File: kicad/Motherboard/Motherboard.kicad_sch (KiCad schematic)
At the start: 72 parts, among them J1 USB_C_Receptacle_USB2.0, J10 Conn_01x08_Pin, J11 Conn_01x08_Pin, J12 Conn_01x08_Pin, J13 Conn_01x08_Pin, J2 Conn_01x02_Pin, J3 Conn_01x04_Pin, J4 Conn_01x04_Pin, J5 Conn_01x02_Pin, J6 Conn_01x08_Pin, J7 Conn_01x08_Pin, J8 Conn_01x08_Pin, J9 Conn_01x08_Pin, Q1 DMN3404L, SW1 Reset, SW2 Boot, U1 ESP32-S2-SOLO, U2 LD1117S33TR_SOT223, U3 TCA9535RTWR, U4 TCA9535RTWR, U5 TCA9535RTWR, U6 TCA9535RTWR, U7 TMC2209-LA, U8 TMC2209-LA, U9 LM2575-5.0BT

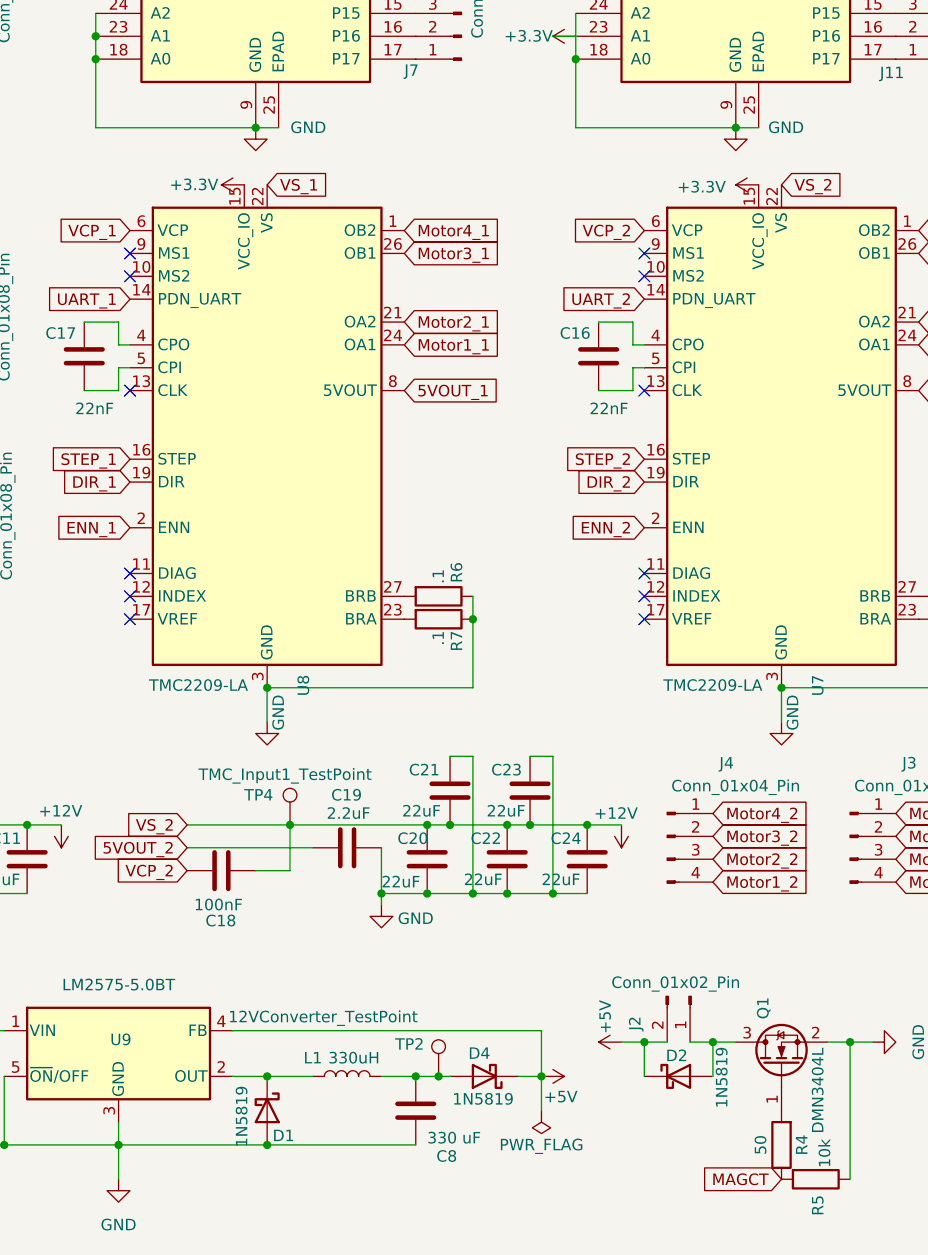
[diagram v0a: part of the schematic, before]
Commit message: finalized schematic
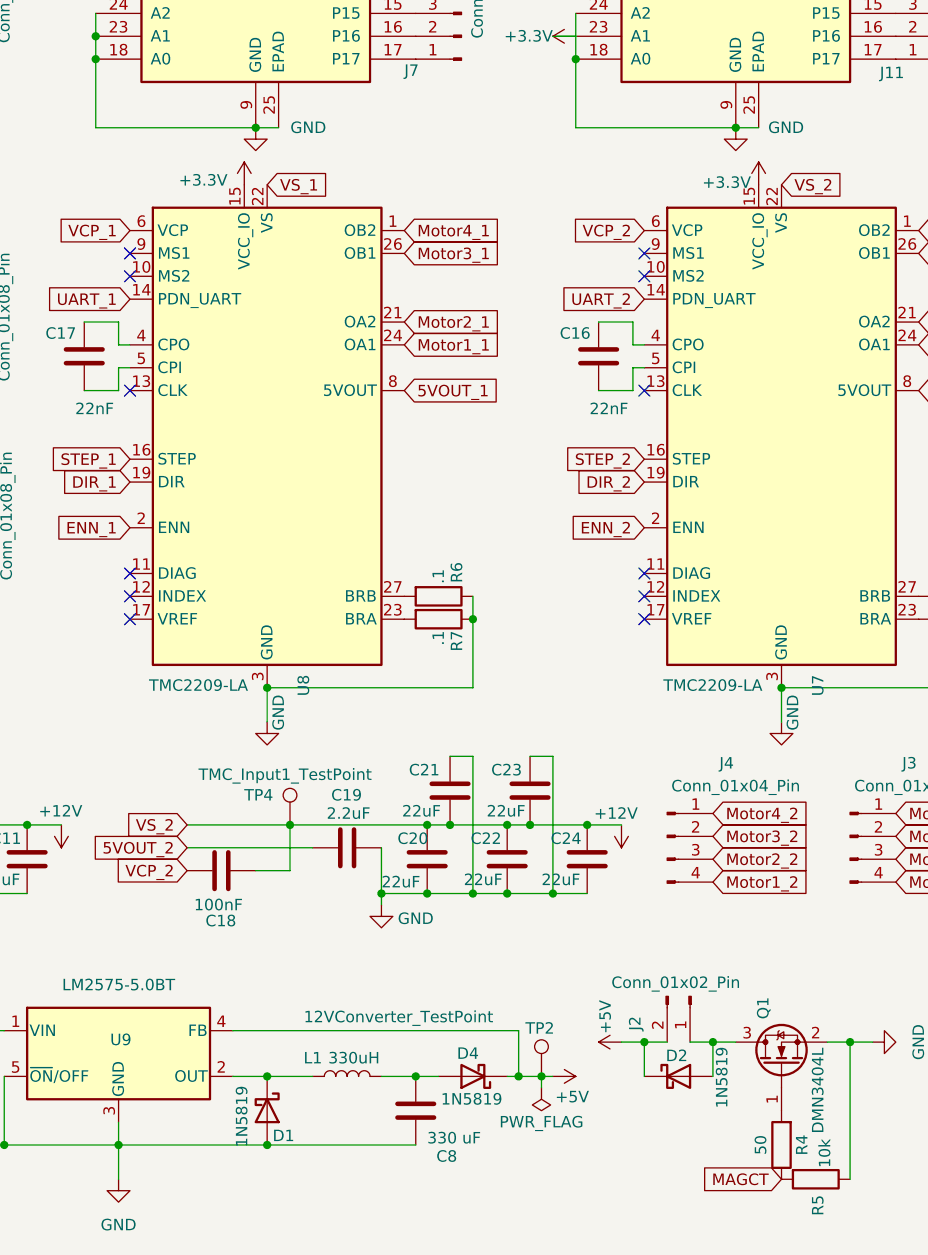
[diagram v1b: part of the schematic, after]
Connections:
- net +5V: now also TP2.1
- net at C8.1, D4.2 (A), L1.2: no longer TP2.1
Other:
- moved on the sheet: D4

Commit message: best layout
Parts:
- removed TP5: TMC_Input2_TestPoint, TestPoint:TestPoint_Pad_1.5x1.5mm, symbol Connector:TestPoint
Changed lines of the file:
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@@
-	)
-	(symbol
-		(lib_id "Connector:TestPoint")
-		(at 36.83 149.86 0)
-		(unit 1)
-		(exclude_from_sim no)
-		(in_bom yes)
-		(on_board yes)
-		(dnp no)
-		(property "Reference" "TP5"
-			(at 31.75 146.812 0)
-			(effects
-				(font
-					(size 1.27 1.27)
-				)
-				(justify left)
-			)
-		)
-		(property "Value" "TMC_Input2_TestPoint"
-			(at 26.416 144.272 0)
-			(effects
-				(font
-					(size 1.27 1.27)
-				)
-				(justify left)
-			)
-		)
-		(property "Footprint" "TestPoint:TestPoint_Pad_1.5x1.5mm"
-			(at 41.91 149.86 0)
-			(effects
-				(font
-					(size 1.27 1.27)
-				)
-				(hide yes)
-			)
-		)
-		(property "Datasheet" "~"
-			(at 41.91 149.86 0)
-			(effects
-				(font
-					(size 1.27 1.27)
-				)
-				(hide yes)
-			)
-		)
-		(property "Description" "test point"
-			(at 36.83 149.86 0)
-			(effects
-				(font
-					(size 1.27 1.27)
-				)
-				(hide yes)
-			)
-		)
-		(pin "1"
-		)
-		(instances
-			(project "Motherboard"
-				(path "/6e7606c8-26d5-4d26-b509-210c4758a44d"
-					(reference "TP5")
-					(unit 1)
-				)
-			)
-		)
 	)
 	(symbol

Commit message: done agian
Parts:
- added H1, H2, H3, H4: MountingHole, symbol Mechanical:MountingHole

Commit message: Done and broke my computer
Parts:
- C7: footprint Capacitor_SMD:C_0805_2012Metric_Pad1.18x1.45mm_HandSolder -> Capacitor_SMD:C_1210_3225Metric_Pad1.33x2.70mm_HandSolder
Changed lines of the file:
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@@
 			)
 		)
-		(property "Footprint" "Capacitor_SMD:C_0805_2012Metric_Pad1.18x1.45mm_HandSolder"
+		(property "Footprint" "Capacitor_SMD:C_1210_3225Metric_Pad1.33x2.70mm_HandSolder"
 			(at 56.8452 182.88 0)
 			(effects

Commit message: FML
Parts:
- U7, U8: footprint Package_DFN_QFN:TQFN-32-1EP_5x5mm_P0.5mm_EP3.4x3.4mm_ThermalVias -> Package_DFN_QFN:TQFN-28-1EP_5x5mm_P0.5mm_EP3.25x3.25mm_ThermalVias
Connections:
- net GND: now also U7.29 (EPAD), U8.29 (EPAD)
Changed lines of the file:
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@@
 	)
 	(junction
+		(at 151.13 134.62)
+		(diameter 0)
+		(color 0 0 0 0)
+	)
+	(junction
 		(at 26.67 179.07)
 		(diameter 0)
@@
 	)
 	(junction
+		(at 96.52 134.62)
+		(diameter 0)
+		(color 0 0 0 0)
+	)
+	(junction
+		(at 154.94 134.62)
+		(diameter 0)
+		(color 0 0 0 0)
+	)
+	(junction
 		(at 77.47 64.77)
 		(diameter 0)
@@
 	)
 	(junction
+		(at 97.79 134.62)
+		(diameter 0)
+		(color 0 0 0 0)
+	)
+	(junction
 		(at 96.52 185.42)
 		(diameter 0)
@@
 	)
 	(junction
+		(at 93.98 134.62)
+		(diameter 0)
+		(color 0 0 0 0)
+	)
+	(junction
 		(at 240.03 24.13)
 		(diameter 0)
@@
 	)
 	(junction
-		(at 153.67 134.62)
-		(diameter 0)
-		(color 0 0 0 0)
-	)
-	(junction
 		(at 124.46 177.8)
 		(diameter 0)
@@
 	)
 	(junction
-		(at 119.38 157.48)
+		(at 153.67 134.62)
 		(diameter 0)
 		(color 0 0 0 0)
 	)
 	(junction
-		(at 96.52 134.62)
+		(at 119.38 157.48)
 		(diameter 0)
 		(color 0 0 0 0)
@@
 	(wire
 		(pts
+			(xy 147.32 134.62) (xy 151.13 134.62)
+		)
+		(stroke
+			(width 0)
+			(type default)
+		)
+	)
+	(wire
+		(pts
+			(xy 97.79 134.62) (xy 119.38 134.62)
+		)
+		(stroke
+			(width 0)
+			(type default)
+		)
+	)
+	(wire
+		(pts
 			(xy 227.33 31.75) (xy 227.33 36.83)
 		)
@@
 	(wire
 		(pts
+			(xy 154.94 134.62) (xy 176.53 134.62)
+		)
+		(stroke
+			(width 0)
+			(type default)
+		)
+	)
+	(wire
+		(pts
 			(xy 124.46 172.72) (xy 124.46 177.8)
 		)
@@
 	(wire
 		(pts
-			(xy 132.08 149.86) (xy 135.89 149.86)
+			(xy 90.17 134.62) (xy 93.98 134.62)
 		)
 		(stroke
@@
 	(wire
 		(pts
-			(xy 201.93 33.02) (xy 199.39 33.02)
+			(xy 132.08 149.86) (xy 135.89 149.86)
 		)
 		(stroke
@@
 	(wire
 		(pts
-			(xy 119.38 134.62) (xy 96.52 134.62)
+			(xy 201.93 33.02) (xy 199.39 33.02)
 		)
 		(stroke
@@
 	(wire
 		(pts
+			(xy 93.98 134.62) (xy 96.52 134.62)
+		)
+		(stroke
+			(width 0)
+			(type default)
+		)
+	)
+	(wire
+		(pts
 			(xy 182.88 138.43) (xy 191.77 138.43)
 		)
@@
 	(wire
 		(pts
-			(xy 176.53 134.62) (xy 153.67 134.62)
+			(xy 259.08 152.4) (xy 259.08 154.94)
 		)
 		(stroke
@@
 	(wire
 		(pts
-			(xy 259.08 152.4) (xy 259.08 154.94)
+			(xy 151.13 134.62) (xy 153.67 134.62)
 		)
 		(stroke
@@
 	(wire
 		(pts
+			(xy 96.52 134.62) (xy 97.79 134.62)
+		)
+		(stroke
+			(width 0)
+			(type default)
+		)
+	)
+	(wire
+		(pts
 			(xy 55.88 182.88) (xy 55.88 185.42)
 		)
@@
 	(wire
 		(pts
+			(xy 153.67 134.62) (xy 154.94 134.62)
+		)
+		(stroke
+			(width 0)
+			(type default)
+		)
+	)
+	(wire
+		(pts
 			(xy 109.22 158.75) (xy 109.22 157.48)
 		)
@@
 			)
 		)
-		(property "Footprint" "Package_DFN_QFN:TQFN-32-1EP_5x5mm_P0.5mm_EP3.4x3.4mm_ThermalVias"
+		(property "Footprint" "Package_DFN_QFN:TQFN-28-1EP_5x5mm_P0.5mm_EP3.25x3.25mm_ThermalVias"
 			(at 153.67 147.32 0)
 			(effects
@@
 		(pin "7"
 		)
+		(pin "29"
+		)
 		(instances
 			(project "Motherboard"
@@
 			)
 		)
-		(property "Footprint" "Package_DFN_QFN:TQFN-32-1EP_5x5mm_P0.5mm_EP3.4x3.4mm_ThermalVias"
+		(property "Footprint" "Package_DFN_QFN:TQFN-28-1EP_5x5mm_P0.5mm_EP3.25x3.25mm_ThermalVias"
 			(at 96.52 147.32 0)
 			(effects
@@
 		(pin "7"
 		)
+		(pin "29"
+		)
 		(instances

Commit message: added new parts
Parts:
- removed H1, H2, H3, H4: MountingHole, symbol Mechanical:MountingHole
- added U10, U11: TMC2209-LA, Package_DFN_QFN:VQFN-28-1EP_5x5mm_P0.5mm_EP3.7x3.7mm_ThermalVias, symbol Driver_Motor:TMC2209-LA
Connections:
- net GND: no longer U3.18 (A0), U3.23 (A1), U3.24 (A2), U3.25 (EPAD), U4.18 (A0), U4.23 (A1), U4.25 (EPAD), U5.18 (A0), U5.24 (A2), U5.25 (EPAD), U6.23 (A1), U6.24 (A2), U6.25 (EPAD)
- new net: U4.18 (A0), U4.23 (A1), U4.25 (EPAD)
- new net: U6.23 (A1), U6.24 (A2), U6.25 (EPAD)
- new net: U5.18 (A0), U5.24 (A2), U5.25 (EPAD)
- new net: U10.18 (GND), U10.29 (GND), U10.3 (GND)
- new net: U10.22 (VS), U10.28 (VS)
- new net: U11.18 (GND), U11.29 (GND), U11.3 (GND)
- new net: U11.22 (VS), U11.28 (VS)
- new net: U3.18 (A0), U3.23 (A1), U3.24 (A2), U3.25 (EPAD)
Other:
- note added: "GPIO EXPANDERS"
- moved on the sheet: C10, C11, C12, C13, C14, C15, C16, C17, C18, C19, C20, C21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
